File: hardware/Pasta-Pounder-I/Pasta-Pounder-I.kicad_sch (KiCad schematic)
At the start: 2 parts, among them J1 USB_C_Receptacle, U1 ESP32-WROOM-32E

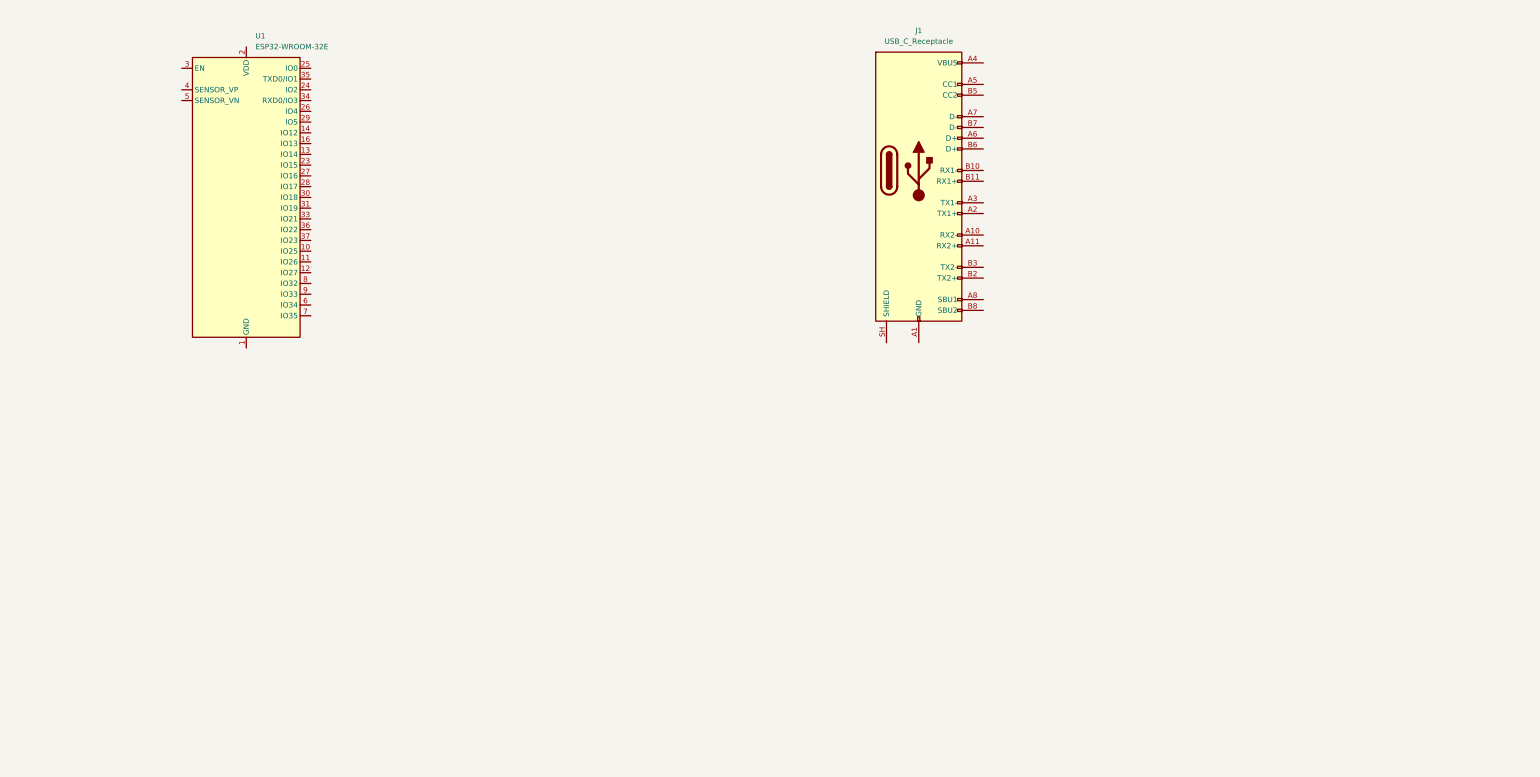
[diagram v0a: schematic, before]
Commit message: Finished USB-C Port Schematic
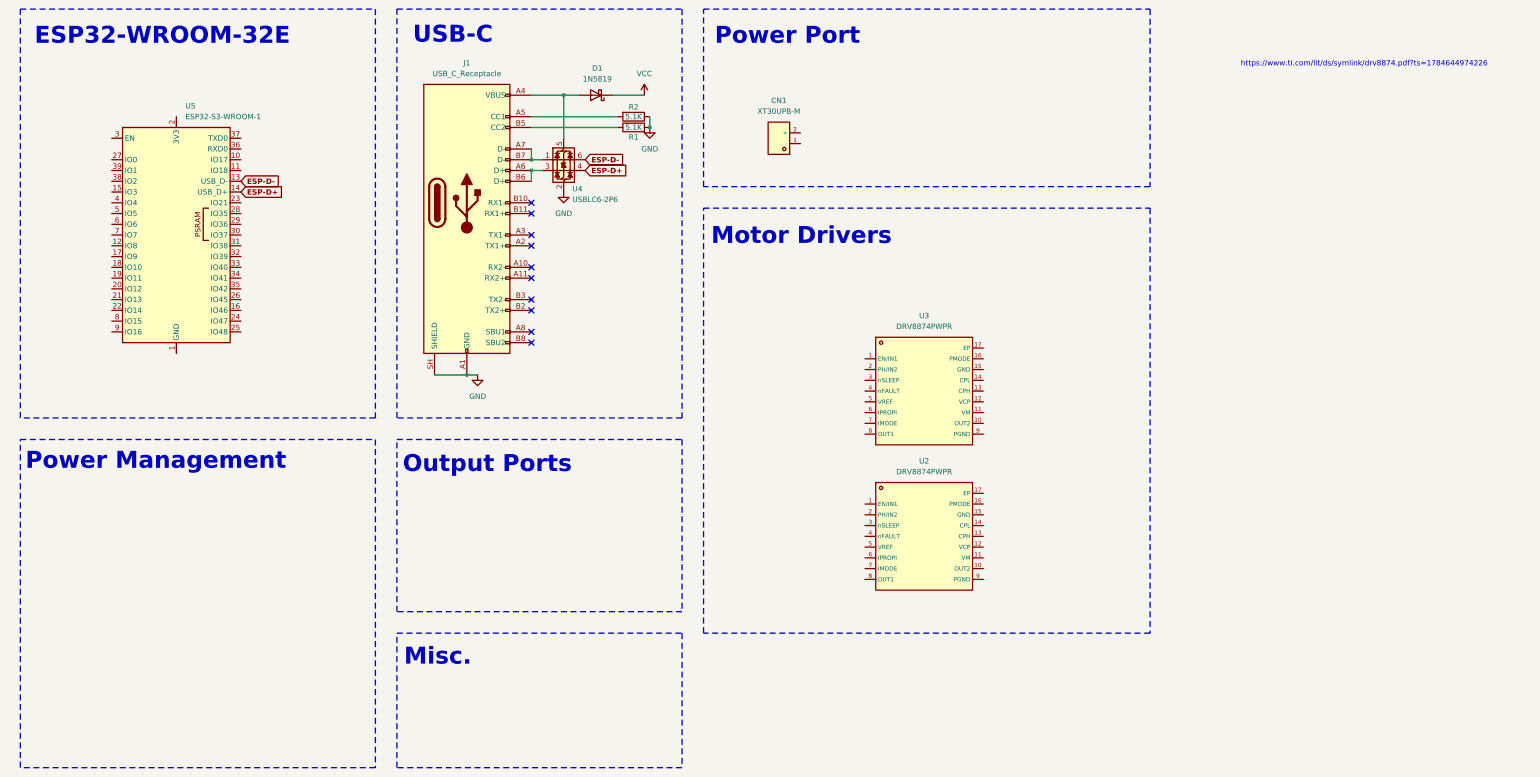
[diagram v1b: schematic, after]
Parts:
- removed U1: ESP32-WROOM-32E, RF_Module:ESP32-WROOM-32D, symbol RF_Module:ESP32-WROOM-32E
- added CN1: XT30UPB-M, lcsc_footprints:C428721_CONN-TH_XT30UPB-M, symbol lcsc_imported:XT30UPB-M
- added D1: 1N5819, Diode_THT:D_DO-41_SOD81_P10.16mm_Horizontal, symbol Diode:1N5819
- added R1, R2: 5.1K, symbol Device:R
- added U2, U3: DRV8874PWPR, lcsc_footprints:C1855818_HTSSOP-16_L5_0-W4_4-P0_65-LS6_4-BL-EP, symbol lcsc_imported:DRV8874PWPR
- added U4: USBLC6-2P6, Package_TO_SOT_SMD:SOT-666, symbol Power_Protection:USBLC6-2P6
- added U5: ESP32-S3-WROOM-1, RF_Module:ESP32-S3-WROOM-1, symbol RF_Module:ESP32-S3-WROOM-1
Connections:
- net GND: now reaches J1.A1 (GND), J1.A12 (GND), J1.B1 (GND), J1.B12 (GND)
- net GND: now also J1.SH (SHIELD), R1.2, R2.1, U4.2 (GND)
- net at J1.A4 (VBUS), J1.A9 (VBUS), J1.B4 (VBUS)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: now also D1.2 (A), U4.5 (VBUS)
- net at J1.A5 (CC1): now also R2.2
- net at J1.A6 (D+): now also J1.B6 (D+), U4.3 (I/O2)
- net at J1.A7 (D-): now also J1.B7 (D-), U4.1 (I/O1)
- net at J1.B5 (CC2): now also R1.1
- new net: U5.1 (GND), U5.40 (GND), U5.41 (GND)
- new net ESP-D+: U4.4 (I/O2), U5.14 (USB_D+)
- new net ESP-D-: U4.6 (I/O1), U5.13 (USB_D-)
- new net VCC: D1.1 (K)
- no-connect marks 0 -> 10
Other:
- note added: "ESP32-WROOM-32E"
- note added: "Misc."
- note added: "Motor Drivers"
- note added: "Output Ports"
- note added: "Power Management"
- note added: "Power Port"
- note added: "USB-C"
- note added: "https://www.ti.com/lit/ds/symlink/drv8874.pdf?ts=1784644974226"
- title: (none) -> Pasta Pounder I
- moved on the sheet: J1
